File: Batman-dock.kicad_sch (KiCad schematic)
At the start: 5 parts, among them J1 TYPEC-324-BCP24, J2 70AAJ-6-M0G, J3 70AAJ-6-M0G

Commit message: Kicad 9. Added usb and spring footprint.
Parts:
- J1: footprint part:TYPE-C-31-M-04 -> jlc:USB-TYPE-C-SMD_USB-307HG-B-SU; LCSC C2835314 -> C309352
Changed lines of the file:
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@@
 (kicad_sch
-	(version 20231120)
+	(version 20250114)
 	(generator "eeschema")
-	(generator_version "8.0")
+	(generator_version "9.0")
 	(paper "A4")
 	(junction
@@
 			)
 		)
-		(property "Footprint" "part:TYPE-C-31-M-04"
+		(property "Footprint" "jlc:USB-TYPE-C-SMD_USB-307HG-B-SU"
 			(at 199.39 85.09 0)
 			(effects
@@
 			)
 		)
-		(property "Datasheet" "https://www.usb.org/sites/default/files/documents/usb_type-c.zip"
+		(property "Datasheet" "https://wmsc.lcsc.com/wmsc/upload/file/pdf/v2/lcsc/1912111437_HOOYA-USB-307HG-B-SU_C309352.pdf"
 			(at 199.39 85.09 0)
 			(effects
@@
 			)
 		)
-		(property "Description" ""
+		(property "Description" "C2835314 would be too high"
 			(at 203.2 85.09 0)
 			(effects
@@
 			)
 		)
-		(property "LCSC" "C2835314"
+		(property "LCSC" "C309352"
 			(at 203.2 85.09 0)
 			(effects
@@
 		)
 	)
+	(embedded_fonts no)
 )

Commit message: Batman routing
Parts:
- J1: value TYPEC-324-BCP24 -> TYPECL324LBCP24
- J2, J3: value 70AAJ-6-M0G -> 70AAJL6LM0G
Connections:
- net +12V is gone; now on net VBUS: J1.A4 (VBUS), J1.A9 (VBUS), J1.B4 (VBUS), J1.B9 (VBUS)
- net CAN0_H: now also J3.4, J3.9
- net CAN0_L: now also J3.10, J3.3
- net CAN1_H: now also J2.5, J2.8
- net CAN1_L: now also J2.6, J2.7
- net CAN2_H: now also J2.10, J2.3
- net CAN2_L: now also J2.4, J2.9
- net CAN3_H: now also J3.11, J3.2
- net CAN3_L: now also J3.1, J3.12
- net GND: now also J3.6, J3.7
- net SBU1: now also J3.5, J3.8
- net SBU2: now also J2.11, J2.2
- net VBUS: now reaches J2.1
- net VBUS: now also J2.12
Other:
- moved on the sheet: J2, J3

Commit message: 1mm batman PCB
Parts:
- J1: footprint jlc:USB-TYPE-C-SMD_USB-307HG-B-SU -> jlc:USB-SMD_HC-TYPE-C-24P-CP1.0-5A-L10.45-01; FT Rotation Offset (none) -> 180; LCSC C309352 -> C5345938
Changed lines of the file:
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@@
 			)
 		)
-		(property "Footprint" "jlc:USB-TYPE-C-SMD_USB-307HG-B-SU"
+		(property "Footprint" "jlc:USB-SMD_HC-TYPE-C-24P-CP1.0-5A-L10.45-01"
 			(at 199.39 85.09 0)
 			(effects
@@
 			)
 		)
-		(property "LCSC" "C309352"
+		(property "LCSC" "C5345938"
 			(at 203.2 85.09 0)
 			(effects
+				(font
+					(size 1.27 1.27)
+				)
+				(hide yes)
+			)
+		)
+		(property "FT Rotation Offset" "180"
+			(at 203.2 85.09 0)
+			(effects

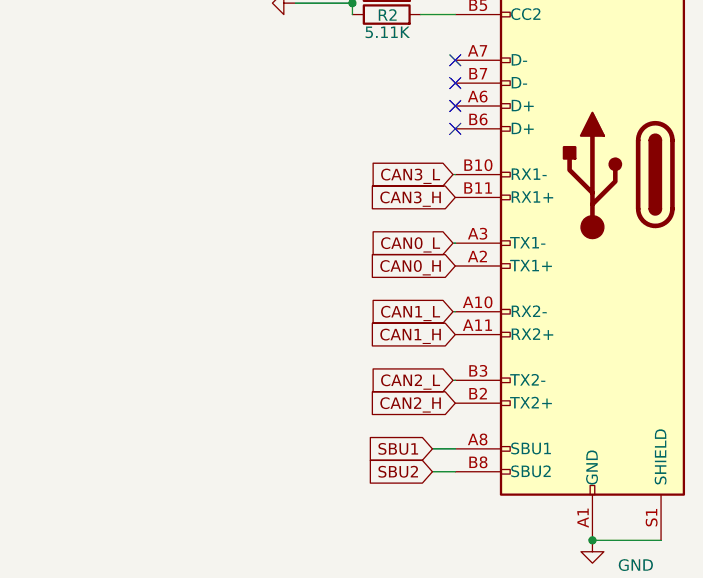
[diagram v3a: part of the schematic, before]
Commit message: Fixed CAN order RX<->TX flip. Less copper.
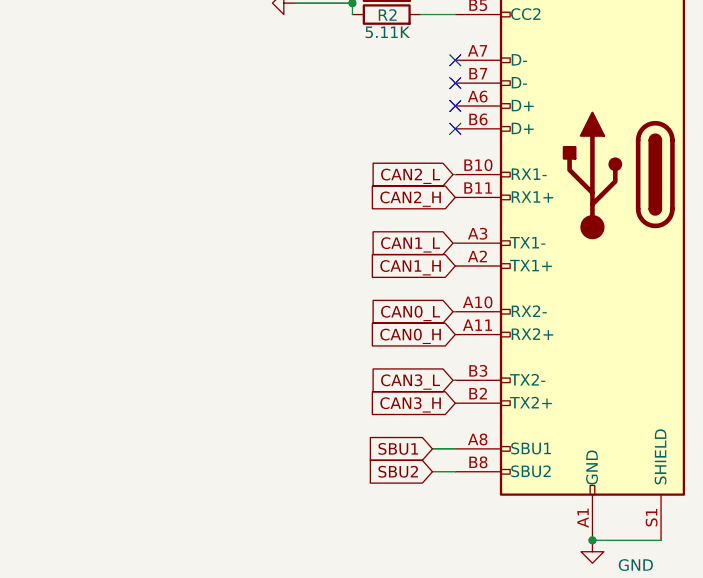
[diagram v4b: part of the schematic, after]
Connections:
- net CAN0_H: now also J1.A11 (RX2+); no longer J1.A2 (TX1+)
- net CAN0_L: now also J1.A10 (RX2-); no longer J1.A3 (TX1-)
- net CAN1_H: now also J1.A2 (TX1+); no longer J1.A11 (RX2+)
- net CAN1_L: now also J1.A3 (TX1-); no longer J1.A10 (RX2-)
- net CAN2_H: now also J1.B11 (RX1+); no longer J1.B2 (TX2+)
- net CAN2_L: now also J1.B10 (RX1-); no longer J1.B3 (TX2-)
- net CAN3_H: now also J1.B2 (TX2+); no longer J1.B11 (RX1+)
- net CAN3_L: now also J1.B3 (TX2-); no longer J1.B10 (RX1-)
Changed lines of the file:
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@@
+		)
+	)
+	(global_label "SBU2"
+		(shape input)
+		(at 185.42 118.11 180)
+		(fields_autoplaced yes)
+		(effects
+			(font
+				(size 1.27 1.27)
+			)
+			(justify right)
+		)
+		(property "Intersheetrefs" "${INTERSHEET_REFS}"
+			(at 177.4153 118.11 0)
+			(effects
+				(font
+					(size 1.27 1.27)
+				)
+				(justify right)
+				(hide yes)
+			)
 		)
 	)
 	(global_label "CAN0_H"
 		(shape input)
+		(at 187.96 102.87 180)
+		(fields_autoplaced yes)
+		(effects
+			(font
+				(size 1.27 1.27)
+			)
+			(justify right)
+		)
+		(property "Intersheetrefs" "${INTERSHEET_REFS}"
+			(at 177.8575 102.87 0)
+			(effects
+				(font
+					(size 1.27 1.27)
+				)
+				(justify right)
+				(hide yes)
+			)
+		)
+	)
+	(global_label "CAN0_L"
+		(shape input)
+		(at 187.706 100.33 180)
+		(fields_autoplaced yes)
+		(effects
+			(font
+				(size 1.27 1.27)
+			)
+			(justify right)
+		)
+		(property "Intersheetrefs" "${INTERSHEET_REFS}"
+			(at 177.9059 100.33 0)
+			(effects
+				(font
+					(size 1.27 1.27)
+				)
+				(justify right)
+				(hide yes)
+			)
+		)
+	)
+	(global_label "CAN1_L"
+		(shape input)
+		(at 187.706 92.71 180)
+		(fields_autoplaced yes)
+		(effects
+			(font
+				(size 1.27 1.27)
+			)
+			(justify right)
+		)
+		(property "Intersheetrefs" "${INTERSHEET_REFS}"
+			(at 177.9059 92.71 0)
+			(effects
+				(font
+					(size 1.27 1.27)
+				)
+				(justify right)
+				(hide yes)
+			)
+		)
+	)
+	(global_label "CAN3_H"
+		(shape input)
+		(at 187.96 110.49 180)
+		(fields_autoplaced yes)
+		(effects
+			(font
+				(size 1.27 1.27)
+			)
+			(justify right)
+		)
+		(property "Intersheetrefs" "${INTERSHEET_REFS}"
+			(at 177.7781 110.49 0)
+			(effects
+				(font
+					(size 1.27 1.27)
+				)
+				(justify right)
+				(hide yes)
+			)
+		)
+	)
+	(global_label "CAN1_H"
+		(shape input)
 		(at 187.96 95.25 180)
 		(fields_autoplaced yes)
@@
 		)
 	)
+	(global_label "CAN2_L"
+		(shape input)
+		(at 187.706 85.09 180)
+		(fields_autoplaced yes)
+		(effects
+			(font
+				(size 1.27 1.27)
+			)
+			(justify right)
+		)
+		(property "Intersheetrefs" "${INTERSHEET_REFS}"
+			(at 177.8265 85.09 0)
+			(effects
+				(font
+					(size 1.27 1.27)
+				)
+				(justify right)
+				(hide yes)
+			)
+		)
+	)
+	(global_label "SBU1"
+		(shape input)
+		(at 185.42 115.57 180)
+		(fields_autoplaced yes)
+		(effects
+			(font
+				(size 1.27 1.27)
+			)
+			(justify right)
+		)
+		(property "Intersheetrefs" "${INTERSHEET_REFS}"
+			(at 177.4153 115.57 0)
+			(effects
+				(font
+					(size 1.27 1.27)
+				)
+				(justify right)
+				(hide yes)
+			)
+		)
+	)
+	(global_label "CAN3_L"
+		(shape input)
+		(at 187.706 107.95 180)
+		(fields_autoplaced yes)
+		(effects
+			(font
+				(size 1.27 1.27)
+			)
+			(justify right)
+		)
+		(property "Intersheetrefs" "${INTERSHEET_REFS}"
+			(at 177.8265 107.95 0)
+			(effects
+				(font
+					(size 1.27 1.27)
+				)
+				(justify right)
+				(hide yes)
+			)
+		)
+	)
 	(global_label "CAN2_H"
 		(shape input)
-		(at 187.96 110.49 180)
-		(fields_autoplaced yes)
-		(effects
-			(font
-				(size 1.27 1.27)
-			)
-			(justify right)
-		)
-		(property "Intersheetrefs" "${INTERSHEET_REFS}"
-			(at 177.7781 110.49 0)
-			(effects
-				(font
-					(size 1.27 1.27)
-				)
-				(justify right)
-				(hide yes)
-			)
-		)
-	)
-	(global_label "SBU2"
-		(shape input)
-		(at 185.42 118.11 180)
-		(fields_autoplaced yes)
-		(effects
-			(font
-				(size 1.27 1.27)
-			)
-			(justify right)
-		)
-		(property "Intersheetrefs" "${INTERSHEET_REFS}"
-			(at 177.4153 118.11 0)
-			(effects
-				(font
-					(size 1.27 1.27)
-				)
-				(justify right)
-				(hide yes)
-			)
-		)
-	)
-	(global_label "CAN0_L"
-		(shape input)
-		(at 187.706 92.71 180)
-		(fields_autoplaced yes)
-		(effects
-			(font
-				(size 1.27 1.27)
-			)
-			(justify right)
-		)
-		(property "Intersheetrefs" "${INTERSHEET_REFS}"
-			(at 177.9059 92.71 0)
-			(effects
-				(font
-					(size 1.27 1.27)
-				)
-				(justify right)
-				(hide yes)
-			)
-		)
-	)
-	(global_label "CAN1_L"
-		(shape input)
-		(at 187.706 100.33 180)
-		(fields_autoplaced yes)
-		(effects
-			(font
-				(size 1.27 1.27)
-			)
-			(justify right)
-		)
-		(property "Intersheetrefs" "${INTERSHEET_REFS}"
-			(at 177.9059 100.33 0)
-			(effects
-				(font
-					(size 1.27 1.27)
-				)
-				(justify right)
-				(hide yes)
-			)
-		)
-	)
-	(global_label "CAN3_L"
-		(shape input)
-		(at 187.706 85.09 180)
-		(fields_autoplaced yes)
-		(effects
-			(font
-				(size 1.27 1.27)
-			)
-			(justify right)
-		)
-		(property "Intersheetrefs" "${INTERSHEET_REFS}"
-			(at 177.8265 85.09 0)
-			(effects
-				(font
-					(size 1.27 1.27)
-				)
-				(justify right)
-				(hide yes)
-			)
-		)
-	)
-	(global_label "CAN3_H"
-		(shape input)
 		(at 187.96 87.63 180)
 		(fields_autoplaced yes)
@@
 			(effects
 				(font
-					(size 1.27 1.27)
-				)
-				(justify right)
-				(hide yes)
-			)
-		)
-	)
-	(global_label "CAN2_L"
-		(shape input)
-		(at 187.706 107.95 180)
-		(fields_autoplaced yes)
-		(effects
-			(font
-				(size 1.27 1.27)
-			)
-			(justify right)
-		)
-		(property "Intersheetrefs" "${INTERSHEET_REFS}"
-			(at 177.8265 107.95 0)
-			(effects
-				(font
-					(size 1.27 1.27)
-				)
-				(justify right)
-				(hide yes)
-			)
-		)
-	)
-	(global_label "SBU1"
-		(shape input)
-		(at 185.42 115.57 180)
-		(fields_autoplaced yes)
-		(effects
-			(font
-				(size 1.27 1.27)
-			)
-			(justify right)
-		)
-		(property "Intersheetrefs" "${INTERSHEET_REFS}"
-			(at 177.4153 115.57 0)
-			(effects
-				(font
-					(size 1.27 1.27)
-				)
-				(justify right)
-				(hide yes)
-			)
-		)
-	)
-	(global_label "CAN1_H"
-		(shape input)
-		(at 187.96 102.87 180)
-		(fields_autoplaced yes)
-		(effects
-			(font
-				(size 1.27 1.27)
-			)
-			(justify right)
-		)
-		(property "Intersheetrefs" "${INTERSHEET_REFS}"
-			(at 177.8575 102.87 0)
-			(effects
-				(font

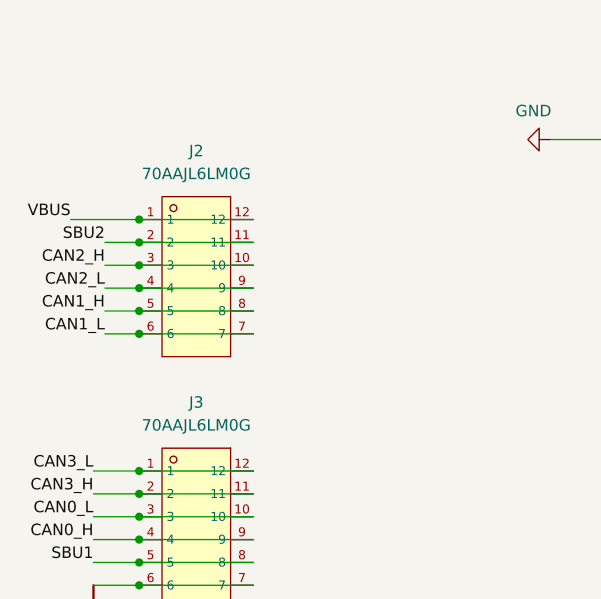
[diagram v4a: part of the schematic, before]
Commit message: Fixed 70AAJ-6-M0G name
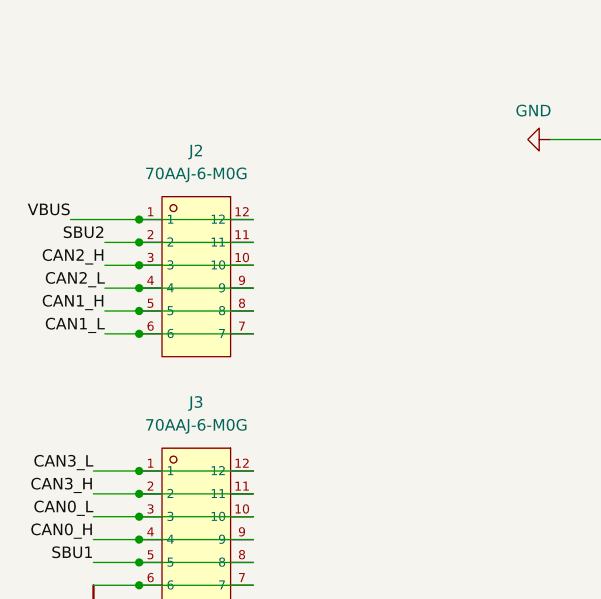
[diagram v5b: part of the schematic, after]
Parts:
- J2, J3: value 70AAJL6LM0G -> 70AAJ-6-M0G
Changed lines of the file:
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@@
 			)
 		)
-		(property "Value" "70AAJL6LM0G"
+		(property "Value" "70AAJ-6-M0G"
 			(at 130.81 69.85 90)
 			(effects
@@
 			)
 		)
-		(property "Value" "70AAJL6LM0G"
+		(property "Value" "70AAJ-6-M0G"
 			(at 130.81 97.79 90)
 			(effects

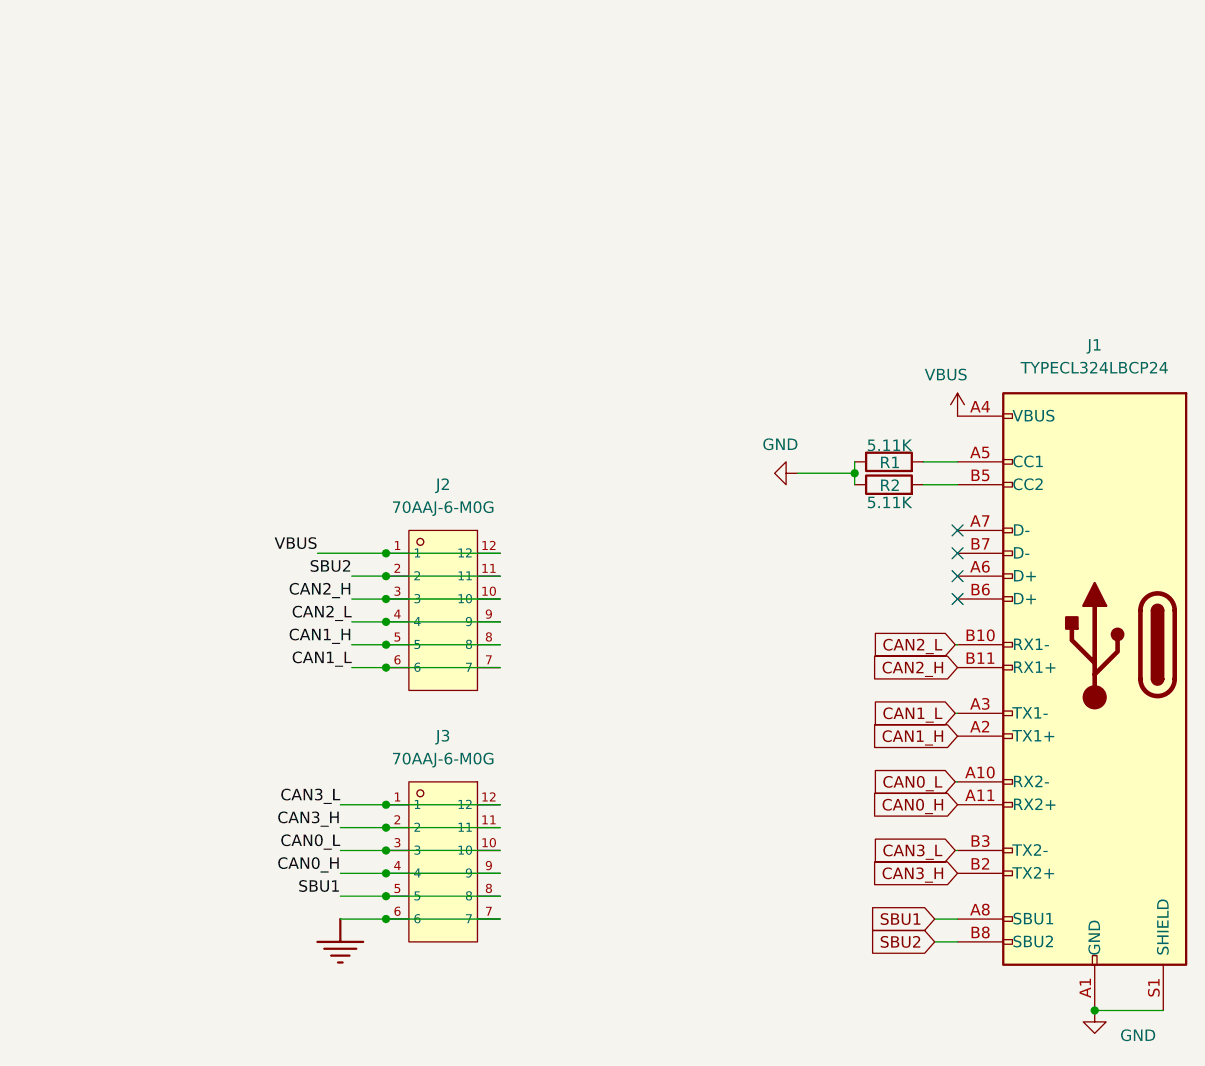
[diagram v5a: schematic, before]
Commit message: Rev.D added anti-reflection resistors and termination footprints. Added through hole test points
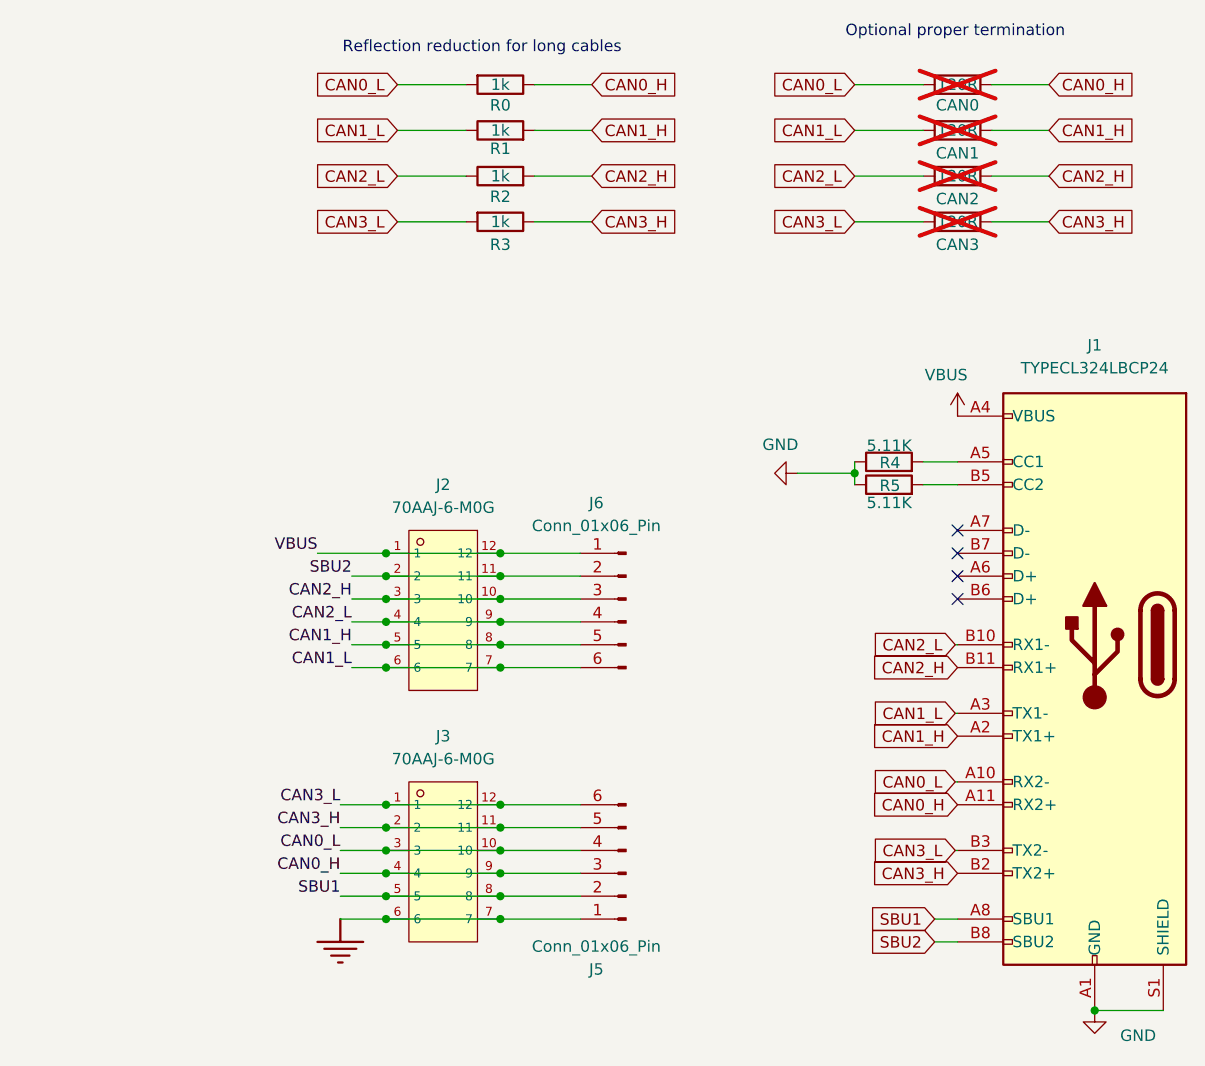
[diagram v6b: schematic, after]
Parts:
- added CAN0, CAN1, CAN2, CAN3: 120R, Resistor_SMD:R_1206_3216Metric_Pad1.30x1.75mm_HandSolder, symbol Device:R
- added J5, J6: Conn_01x06_Pin, Connector_PinHeader_2.54mm:PinHeader_1x06_P2.54mm_Vertical, symbol Connector:Conn_01x06_Pin
- added R0, R1, R2, R3: 1k, Resistor_SMD:R_0603_1608Metric, symbol Device:R
- renumbered R1 to R4, R2 to R5
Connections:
- net CAN0_H: now also CAN0.1, J5.3 (Pin_3), R0.1
- net CAN0_L: now also CAN0.2, J5.4 (Pin_4), R0.2
- net CAN1_H: now also CAN1.1, J6.5 (Pin_5), R1.2
- net CAN1_L: now also CAN1.2, J6.6 (Pin_6), R1.1
- net CAN2_H: now also CAN2.1, J6.3 (Pin_3), R2.2
- net CAN2_L: now also CAN2.2, J6.4 (Pin_4), R2.1
- net CAN3_H: now also CAN3.1, J5.5 (Pin_5), R3.1
- net CAN3_L: now also CAN3.2, J5.6 (Pin_6), R3.2
- net GND: now also J5.1 (Pin_1)
- net SBU1: now also J5.2 (Pin_2)
- net SBU2: now also J6.2 (Pin_2)
- net VBUS: now also J6.1 (Pin_1)
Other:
- note added: "Optional proper termination"
- note added: "Reflection reduction for long cables"

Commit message: PCB remarks and DNP
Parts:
- J5, J6: now left out of the parts list
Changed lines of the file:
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@@
 		(unit 1)
 		(exclude_from_sim no)
-		(in_bom yes)
+		(in_bom no)
 		(on_board yes)
 		(dnp no)
@@
 		(unit 1)
 		(exclude_from_sim no)
-		(in_bom yes)
+		(in_bom no)
 		(on_board yes)
 		(dnp no)
@@
 			)
 		)
-		(property "Datasheet" "https://wmsc.lcsc.com/wmsc/upload/file/pdf/v2/lcsc/1912111437_HOOYA-USB-307HG-B-SU_C309352.pdf"
+		(property "Datasheet" "https://jlcpcb.com/api/file/downloadByFileSystemAccessId/8590908165234520064"
 			(at 199.39 85.09 0)
 			(effects
